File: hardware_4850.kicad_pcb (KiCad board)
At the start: 4 copper layers, 207.2 x 123 mm, 283 parts, among them J101 PWM, J102 ADC, J103 PWM, J104 ADC, J105 +, J106 A, J107 B, J108 C, J109 GND, J1101 HALL, J1102 PWM_EN, J1103 CAN_IN, J1104 CAN_Out, J501 Enable, J601 AIN, J602 USB_B_Mini, J701 MOT_TEMP, P1101 SWD, Q201 NCEP6080AG, Q202 NCEP6080AG, Q203 NCEP6080AG, Q204 NCEP6080AG, Q301 NCEP6080AG, Q302 NCEP6080AG, Q303 NCEP6080AG, Q304 NCEP6080AG, Q401 NCEP6080AG, Q402 NCEP6080AG, Q403 NCEP6080AG, Q404 NCEP6080AG, U1001 GS8632-MR, U1101 TCAN334, U1102 24LC04, U1103 AP2204K-5.0, U201 LM5109BMA, U202 INA240A1PWR, U301 LM5109BMA, U302 INA240A1PWR, U401 LM5109BMA, U402 INA240A1PWR, U501 LMR12010Y, U502 LM5008, U601 STM32F730R8Tx, U701 GS8632-MR, U801 GS8632-MR, U901 GS8632-MR, X601 SM44T

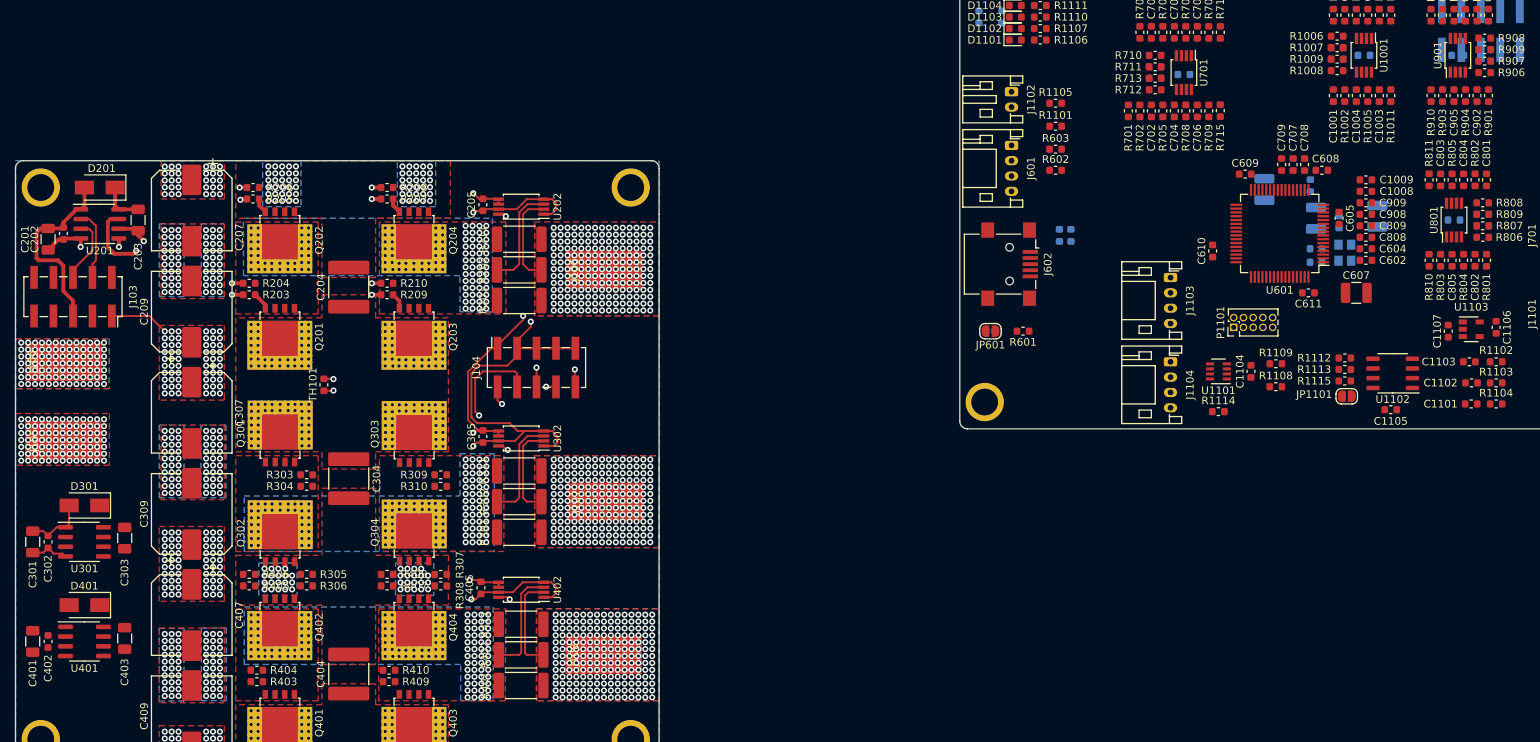
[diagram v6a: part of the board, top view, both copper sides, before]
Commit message: finished power stage routing
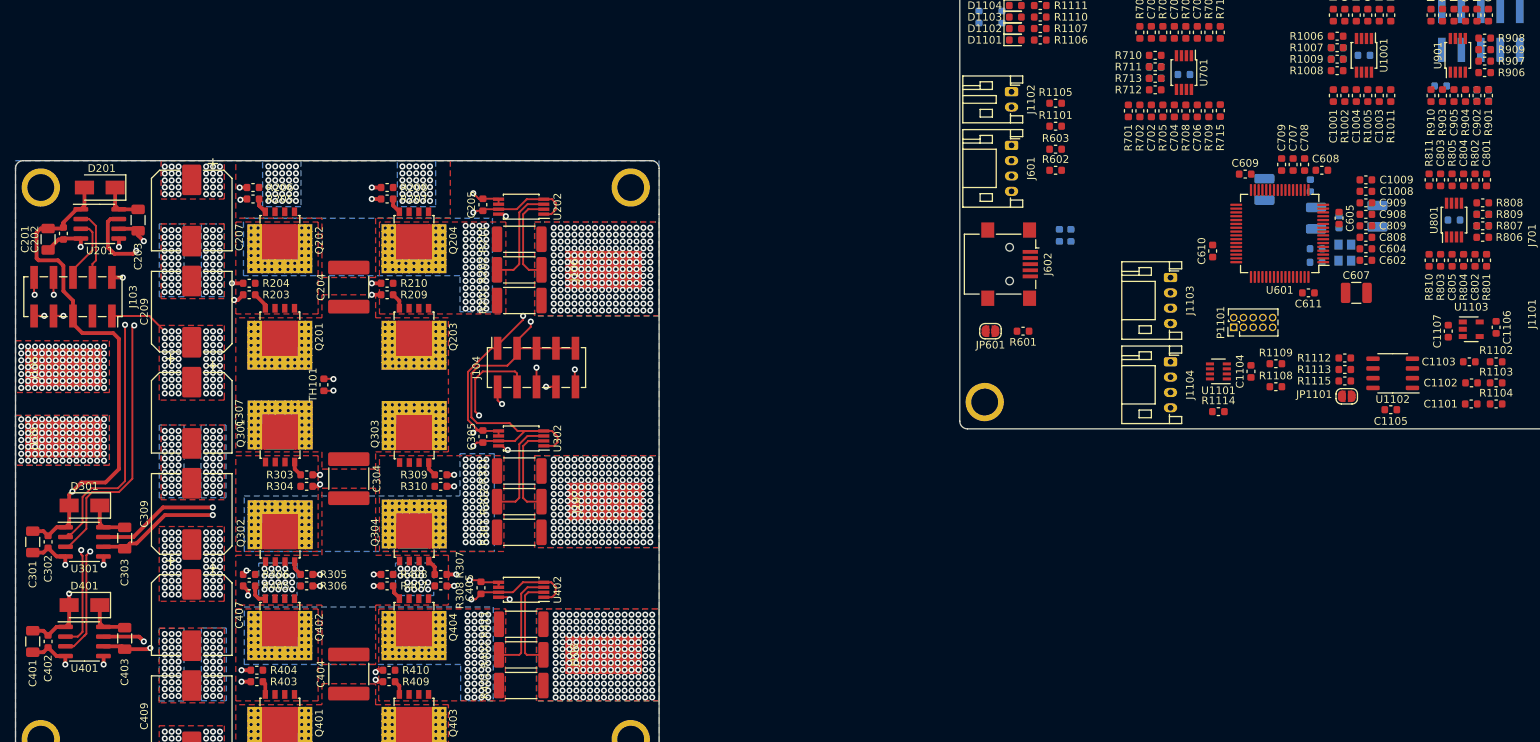
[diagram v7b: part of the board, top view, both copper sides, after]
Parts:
- moved J109 10.0 mm to (63.2, 139.2)
- moved J105 9.50 mm to (63.2, 130.0)
- moved C906 5.26 mm to (248.5, 95.2)
- moved C907 5.26 mm to (248.5, 93.8)
- moved C910 4.59 mm to (243.0, 93.2)
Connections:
- N102 pad 1: GNDPWR -> GNDD
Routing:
- net Net-(C301-Pad2): track 4.99 -> 71.0 mm, vias 0 -> 3
- net Net-(R305-Pad2): track 0.00 -> 59.9 mm, vias 0 -> 3
- net +12P: track 32.8 -> 92.3 mm, vias 0 -> 2
- net Net-(C401-Pad2): track 0.00 -> 59.2 mm, vias 0 -> 3
- net /phase_c/PwmH: track 0.00 -> 55.7 mm, vias 0 -> 2
- net /phase_c/PwmL: track 0.00 -> 54.8 mm, vias 0 -> 2
- net /phase_b/PwmL: track 0.00 -> 52.4 mm, vias 0 -> 2
- net Net-(C303-Pad2): track 0.00 -> 52.3 mm, vias 0 -> 3
- net Net-(R303-Pad2): track 0.00 -> 51.1 mm, vias 0 -> 3
- net Net-(R403-Pad2): track 0.00 -> 49.1 mm, vias 0 -> 3
- net Net-(C403-Pad2): track 0.00 -> 48.7 mm, vias 0 -> 3
- net Net-(R405-Pad2): track 0.00 -> 47.0 mm, vias 0 -> 3
- net /phase_b/PwmH: track 0.00 -> 46.4 mm, vias 0 -> 2
- net Net-(R203-Pad2): track 30.0 -> 50.4 mm
- net Net-(C203-Pad2): track 25.2 -> 45.4 mm
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
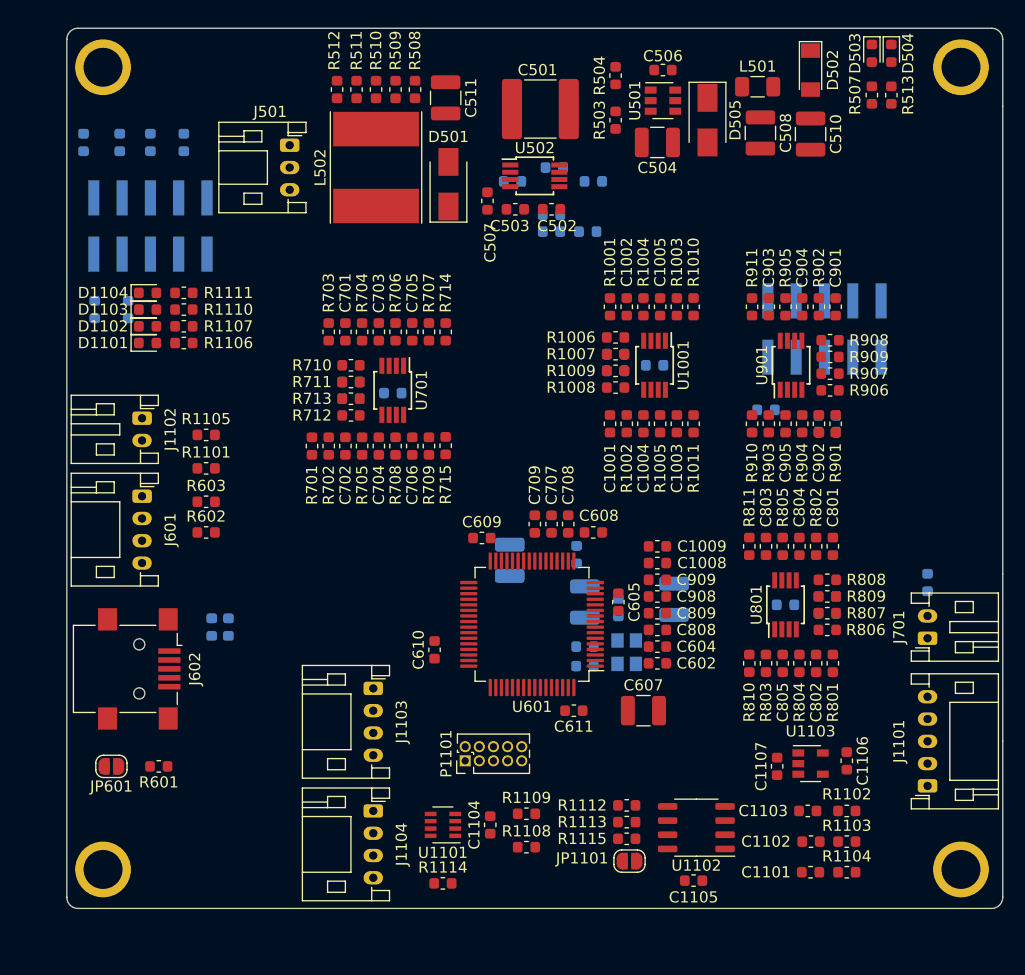
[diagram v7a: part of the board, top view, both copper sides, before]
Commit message: routing of logic supply finished
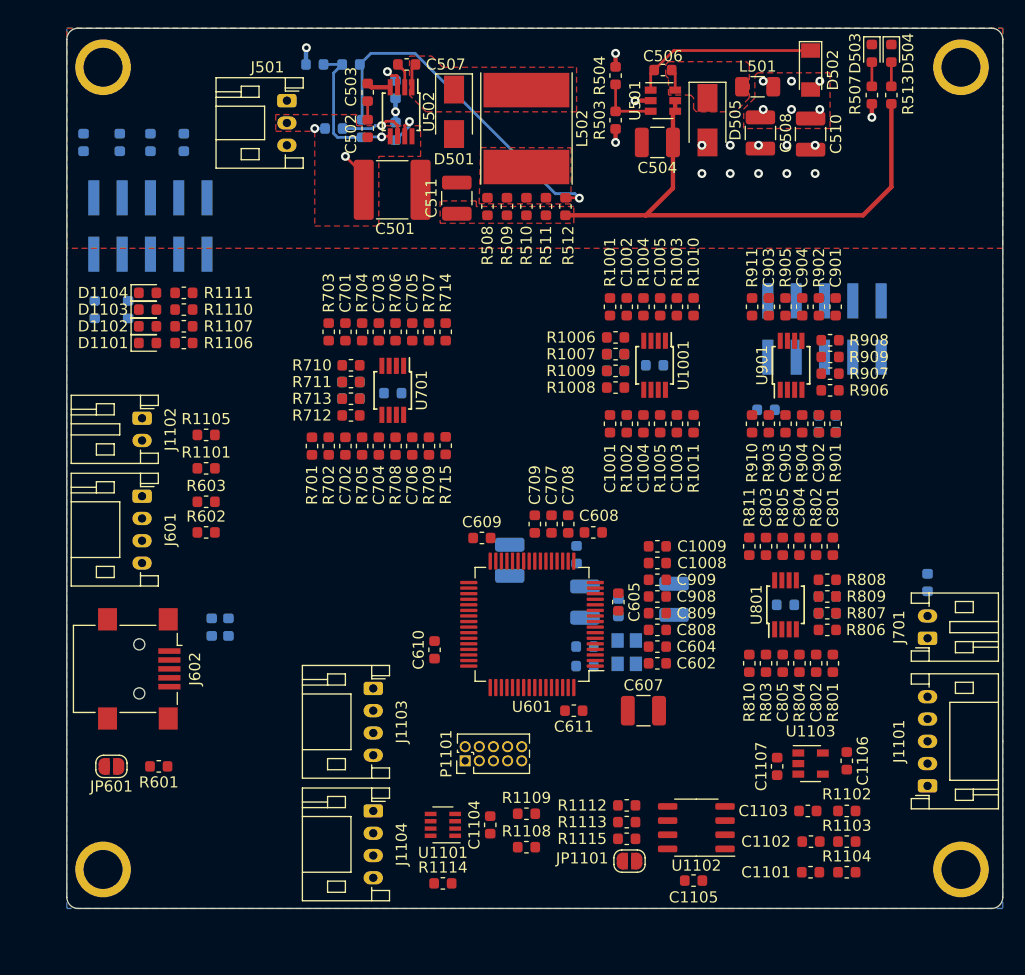
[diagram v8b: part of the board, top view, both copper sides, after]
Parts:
- moved R506 28.7 mm to (202.5, 62.2), turned to 0 degrees
- moved R501 23.8 mm to (204.2, 68.0), turned to 180 degrees
- moved C509 23.4 mm to (205.8, 62.2), turned to 180 degrees
- moved R512 23.0 mm to (225.0, 75.0), turned to 90 degrees
- moved R511 20.0 mm to (223.2, 75.0), turned to 90 degrees
- moved R505 18.7 mm to (206.8, 68.0), turned to 90 degrees
- moved C502 18.0 mm to (207.2, 68.0), turned to 90 degrees
- moved R510 17.1 mm to (221.5, 75.0), turned to 90 degrees
- moved C503 16.9 mm to (207.2, 64.8), turned to 90 degrees
- moved C501 15.1 mm to (209.4, 73.5), turned to 0 degrees
- moved C505 14.6 mm to (209.8, 68.2), turned to 270 degrees
- moved R509 14.5 mm to (219.8, 75.0), turned to 90 degrees
- moved C507 14.2 mm to (210.8, 62.2), turned to 180 degrees
- moved L502 13.9 mm to (221.5, 68.0), turned to 270 degrees
- moved R502 13.4 mm to (209.8, 64.5), turned to 90 degrees
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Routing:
- net +12V: track 0.00 -> 49.1 mm
- net Net-(C509-Pad1): track 0.00 -> 31.8 mm, vias 0 -> 1
- net Net-(C506-Pad2): track 0.00 -> 16.7 mm
- net Net-(C509-Pad2): track 0.00 -> 13.5 mm, vias 0 -> 1
- net GNDD: track 0.00 -> 8.47 mm, vias 0 -> 14
- net Net-(R501-Pad1): track 0.00 -> 6.33 mm, vias 0 -> 1
- net Net-(R503-Pad2): track 0.00 -> 5.58 mm
- net Net-(C501-Pad1): track 0.00 -> 4.61 mm, vias 0 -> 2
- net Net-(C505-Pad2): track 0.00 -> 3.73 mm, vias 0 -> 1
- net Net-(R502-Pad2): track 0.00 -> 3.18 mm, vias 0 -> 1
- net +3V3: track 0.00 -> 2.43 mm, vias 0 -> 8
- net Net-(C507-Pad2): track 0.00 -> 2.30 mm
- net Net-(C507-Pad1): track 0.00 -> 2.18 mm
- net Net-(D504-Pad2): track 0.00 -> 2.18 mm
- net Net-(D503-Pad2): track 0.00 -> 2.18 mm
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- added copper zone on F.Cu, net +12V
- added copper zone on B.Cu, net +3V3
- added copper zone on F.Cu, net +3V3
- added copper zone on F.Cu, net GNDD
- added copper zone on GND, net GNDD
- added copper zone on F.Cu, net Net-(C501-Pad1)
- added copper zone on F.Cu, net Net-(C506-Pad1)
- added copper zone on F.Cu, net Net-(C507-Pad1)
- added copper zone on F.Cu, net Net-(C509-Pad1)
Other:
- net class Dig Supply added: clearance 0.2, trace_width 0.4, via_dia 0.8, via_drill 0.4
